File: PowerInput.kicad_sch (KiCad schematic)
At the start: 17 parts, among them IC301 LM74700QDBVTQ1, J301 1715721, Q301 60V 38A

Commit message: Updated symbols, added jobset and output folders.
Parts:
- C302, C303, C304, C305, C306, C307: Manufacturer (none) -> Samsung Electro-Mechanics; Manufacturer Part No (none) -> CL31A106KBHNNNE
- TP301, TP302, TP303: now left out of the parts list
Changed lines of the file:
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@@
+			)
+		)
+		(property "Manufacturer" "Samsung Electro-Mechanics"
+			(at 147.32 820.65 0)
+			(effects
+				(font
+					(size 1.27 1.27)
+				)
+				(justify left top)
+				(hide yes)
+			)
+		)
+		(property "Manufacturer Part No" "CL31A106KBHNNNE"
+			(at 147.32 920.65 0)
+			(effects
+				(font
+					(size 1.27 1.27)
+				)
+				(justify left top)
+				(hide yes)
 			)
 		)
@@
 		(unit 1)
 		(exclude_from_sim no)
-		(in_bom yes)
+		(in_bom no)
 		(on_board yes)
 		(dnp no)
@@
 		(unit 1)
 		(exclude_from_sim no)
-		(in_bom yes)
+		(in_bom no)
 		(on_board yes)
 		(dnp no)
@@
 			)
 		)
+		(property "Manufacturer" "Samsung Electro-Mechanics"
+			(at 147.32 846.05 0)
+			(effects
+				(font
+					(size 1.27 1.27)
+				)
+				(justify left top)
+				(hide yes)
+			)
+		)
+		(property "Manufacturer Part No" "CL31A106KBHNNNE"
+			(at 147.32 946.05 0)
+			(effects
+				(font
+					(size 1.27 1.27)
+				)
+				(justify left top)
+				(hide yes)
+			)
+		)
 		(pin "2"
 		)
@@
 		(unit 1)
 		(exclude_from_sim no)
-		(in_bom yes)
+		(in_bom no)
 		(on_board yes)
 		(dnp no)
@@
 					(size 1.27 1.27)
 				)
+				(hide yes)
+			)
+		)
+		(property "Manufacturer" "Samsung Electro-Mechanics"
+			(at 147.32 833.35 0)
+			(effects
+				(font
+					(size 1.27 1.27)
+				)
+				(justify left top)
+				(hide yes)
+			)
+		)
+		(property "Manufacturer Part No" "CL31A106KBHNNNE"
+			(at 147.32 933.35 0)
+			(effects
+				(font
+					(size 1.27 1.27)
+				)
+				(justify left top)
 				(hide yes)
 			)
@@
 			)
 		)
+		(property "Manufacturer" "Samsung Electro-Mechanics"
+			(at 147.32 827 0)
+			(effects
+				(font
+					(size 1.27 1.27)
+				)
+				(justify left top)
+				(hide yes)
+			)
+		)
+		(property "Manufacturer Part No" "CL31A106KBHNNNE"
+			(at 147.32 927 0)
+			(effects
+				(font
+					(size 1.27 1.27)
+				)
+				(justify left top)
+				(hide yes)
+			)
+		)
 		(pin "2"
 		)
@@
 			)
 		)
+		(property "Manufacturer" "Samsung Electro-Mechanics"
+			(at 147.32 852.4 0)
+			(effects
+				(font
+					(size 1.27 1.27)
+				)
+				(justify left top)
+				(hide yes)
+			)
+		)
+		(property "Manufacturer Part No" "CL31A106KBHNNNE"
+			(at 147.32 952.4 0)
+			(effects
+				(font
+					(size 1.27 1.27)
+				)
+				(justify left top)
+				(hide yes)
+			)
+		)
 		(pin "2"
 		)
@@
 				(hide yes)
 			)
+		)
+		(property "Manufacturer" "Samsung Electro-Mechanics"
+			(at 147.32 839.7 0)
+			(effects
+				(font
+					(size 1.27 1.27)
+				)
+				(justify left top)
+				(hide yes)
+			)
+		)
+		(property "Manufacturer Part No" "CL31A106KBHNNNE"
+			(at 147.32 939.7 0)
+			(effects
+				(font
+					(size 1.27 1.27)
+				)
+				(justify left top)
+				(hide yes)
+			)

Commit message: Recalculated and reran the USB Lines and impedance. Updated symbols to work in BOM. Ran output.
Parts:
- D301, D302: Package (none) -> SOD-123FL
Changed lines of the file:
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@@
+			)
+		)
+		(property "Package" "SOD-123FL"
+			(at 156.21 75.184 0)
+			(effects
+				(font
+					(size 1.27 1.27)
+				)
+				(hide yes)
 			)
 		)
@@
 			(effects
 				(font
+					(size 1.27 1.27)
+				)
+				(hide yes)
+			)
+		)
+		(property "Package" "SOD-123FL"
+			(at 185.42 54.356 0)
+			(effects
+				(font

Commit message: Updated inductor component and 10uF capacitor components to bring down cost.
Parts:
- removed C302, C303, C304, C305, C306, C307: 10uF 10% 50V, JLCPCB Basic:CAPC3216X180N, symbol JLCPCB Basic:CL31A106KBHNNNE
- added C302, C303, C304, C305, C306, C307: 10uF 10% 25V, JLCPCB Basic:CAPC3216X180N, symbol SAMSUNGELECTROMECHANICS Resistors:CL31A106KAHNNNE
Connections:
- net +12V: now also C302.2, C303.2, C304.2, C305.2, C306.2, C307.2
- net GND: now also C302.1, C303.1, C304.1, C305.1, C306.1, C307.1

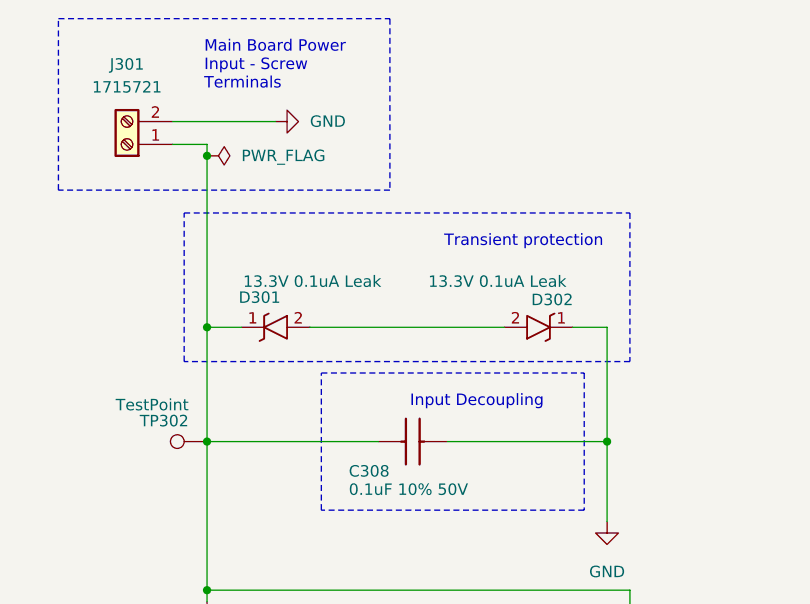
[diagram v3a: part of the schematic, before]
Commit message: Updated the input diode to a TVS that is in stock/normally stocked by JLCPCB
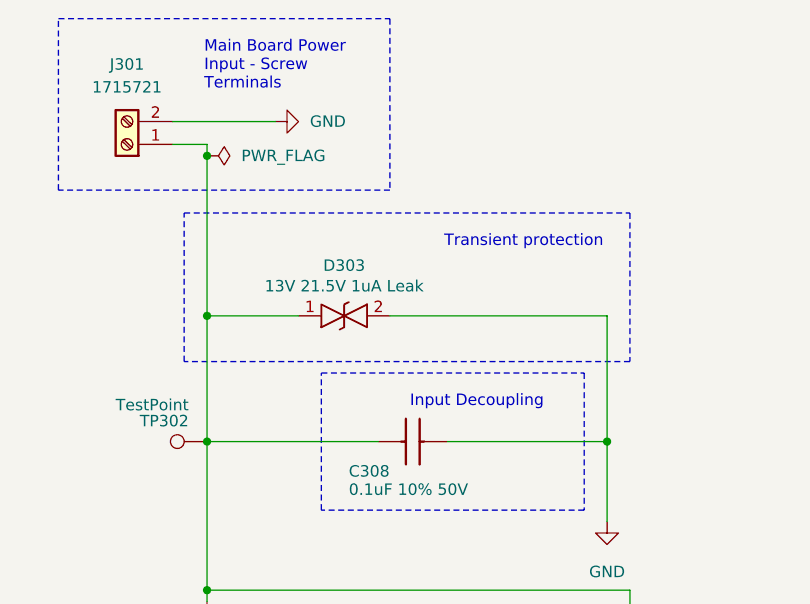
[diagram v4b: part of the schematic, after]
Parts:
- removed D301, D302: 13.3V 0.1uA Leak, LITTELFUSE Diodes:SODFL3619X98N, symbol LITTELFUSE Diodes:SMF4L13AT1G
- added D303: 13V 21.5V 1uA Leak, LITTELFUSE Diodes:DO-214AA_Bidirectional, symbol LITTELFUSE Diodes:SMBJ13CA
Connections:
- net GND: now also D303.2 (A2)
- net at C308.1, C309.1, IC301.3 (EN)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: now also D303.1 (A1)
